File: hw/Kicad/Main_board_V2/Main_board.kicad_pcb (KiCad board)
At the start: 2 copper layers, 100 x 100 mm, 31 parts, among them J1 LIPO 2S, J10 DIST_FRONT, J11 SENSORES_LINEA, J12 DIST_DCHA, J2 MOT_IZQ, J3 TB6612FNG_A, J4 TB6612FNG_B, J5 DC-DC_5V, J6 HC-05, J7 MOT_DER, J8 DIST_IZQ, J9 CAMARA, SW1 SW_DPDT, SW2 SW_Push, SW3 SW_Push, U1 PCF8574

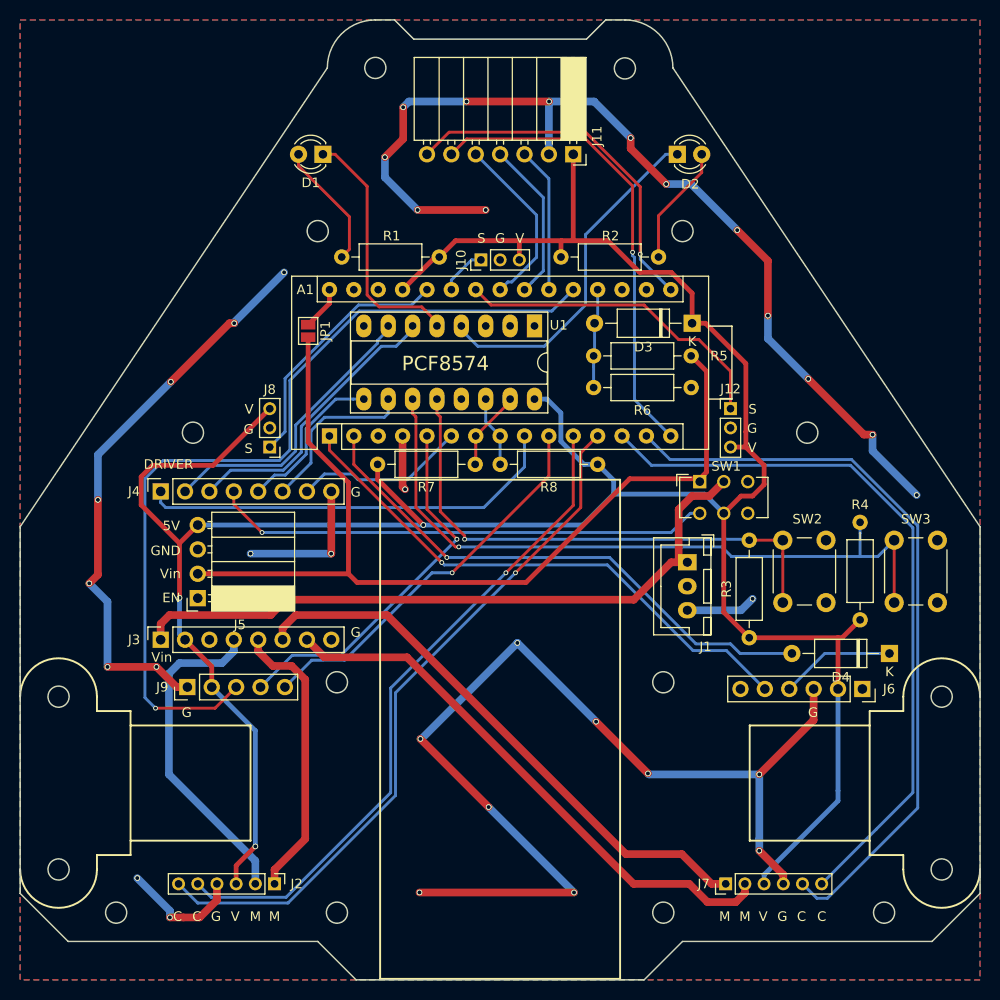
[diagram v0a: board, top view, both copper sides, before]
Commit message: Silkscreen fixed
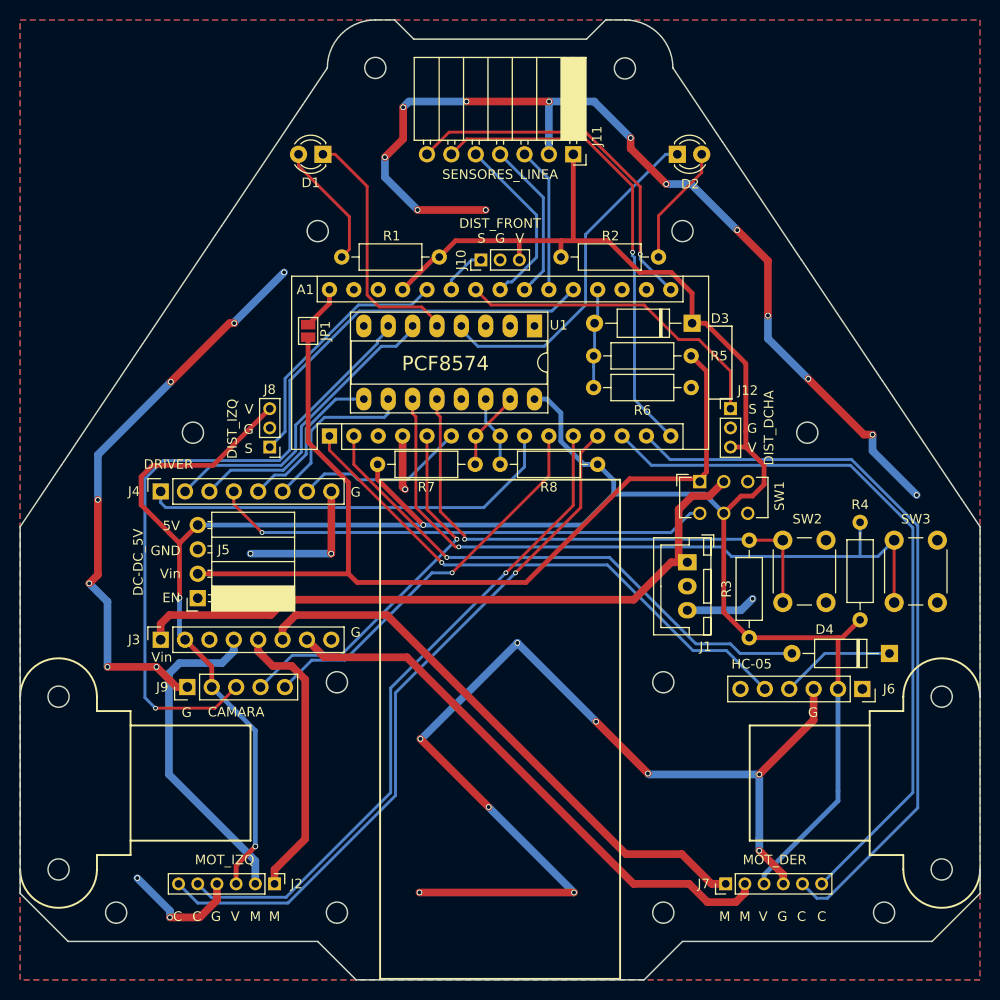
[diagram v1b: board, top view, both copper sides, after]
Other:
- board text added: "CAMARA"
- board text added: "DC-DC_5V"
- board text added: "DIST_DCHA"
- board text added: "DIST_FRONT"
- board text added: "DIST_IZQ"
- board text added: "HC-05"
- board text added: "MOT_DER"
- board text added: "MOT_IZQ"
- board text added: "SENSORES_LINEA"
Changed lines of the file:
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@@
-(kicad_pcb (version 4) (host pcbnew 4.0.7)
+(kicad_pcb (version 4) (host pcbnew 4.0.7+dfsg1-1ubuntu2)
   (general
     (links 94)
     (no_connects 0)
-    (area 99.924999 49.924999 200.075001 150.075001)
+    (area 99.899999 44.8 200.100001 150.100001)
     (thickness 1.6)
-    (drawings 127)
+    (drawings 136)
     (tracks 449)
     (zones 0)
@@
     (47 F.CrtYd user hide)
     (48 B.Fab user hide)
-    (49 F.Fab user hide)
+    (49 F.Fab user)
   )
   (setup
@@
       (effects (font (size 1 1) (thickness 0.15)))
     )
-    (fp_text value MOT_IZQ (at 0 12.06 270) (layer F.Fab)
+    (fp_text value MOT_IZQ (at -2.5 5.2 360) (layer F.Fab)
       (effects (font (size 1 1) (thickness 0.15)))
     )
@@
     (descr "Through hole angled socket strip, 1x04, 2.54mm pitch, 8.51mm socket length, single row (from Kicad 4.0.7), script generated")
     (tags "Through hole angled socket strip THT 1x04 2.54mm single row")
-    (fp_text reference J5 (at -4.38 -2.77 180) (layer F.SilkS)
+    (fp_text reference J5 (at -2.7 5.04 180) (layer F.SilkS)
       (effects (font (size 1 1) (thickness 0.15)))
     )
@@
       (effects (font (size 1 1) (thickness 0.15)))
     )
-    (fp_text value HC-05 (at 0 15.47 270) (layer F.Fab)
+    (fp_text value HC-05 (at -2.6 11.54 360) (layer F.Fab)
       (effects (font (size 1 1) (thickness 0.15)))
     )
@@
       (effects (font (size 1 1) (thickness 0.15)))
     )
-    (fp_text value MOT_DER (at 0 12.06 90) (layer F.Fab)
+    (fp_text value MOT_DER (at 2.5 5.1 180) (layer F.Fab)
       (effects (font (size 1 1) (thickness 0.15)))
     )
@@
       (effects (font (size 1 1) (thickness 0.15)))
     )
-    (fp_text value DIST_IZQ (at 0 6.06 180) (layer F.Fab)
+    (fp_text value DIST_IZQ (at 3.9 1.9 270) (layer F.Fab)
       (effects (font (size 1 1) (thickness 0.15)))
     )
@@
       (effects (font (size 1 1) (thickness 0.15)))
     )
-    (fp_text value CAMARA (at 0 12.49 90) (layer F.Fab)
+    (fp_text value CAMARA (at -2.6 5.08 180) (layer F.Fab)
       (effects (font (size 1 1) (thickness 0.15)))
     )
@@
       (effects (font (size 1 1) (thickness 0.15)))
     )
-    (fp_text value DIST_FRONT (at 0 6.06 90) (layer F.Fab)
+    (fp_text value DIST_FRONT (at 3.8 2 180) (layer F.Fab)
       (effects (font (size 1 1) (thickness 0.15)))
     )
@@
       (effects (font (size 1 1) (thickness 0.15)))
     )
-    (fp_text value SENSORES_LINEA (at -4.38 18.01 270) (layer F.Fab)
+    (fp_text value SENSORES_LINEA (at 2.1 7.62 360) (layer F.Fab)
       (effects (font (size 1 1) (thickness 0.15)))
     )
@@
     (descr "Through hole straight pin header, 1x03, 2.00mm pitch, single row")
     (tags "Through hole pin header THT 1x03 2.00mm single row")
-    (fp_text reference J12 (at 0 -2.06) (layer F.SilkS)
-      (effects (font (size 1 1) (thickness 0.15)))
-    )
-    (fp_text value DIST_DCHA (at 0 6.06) (layer F.Fab)
+    (fp_text reference J12 (at 1.8 -1.9) (layer F.SilkS)
+      (effects (font (size 1 1) (thickness 0.15)))
+    )
+    (fp_text value DIST_DCHA (at 4 2 90) (layer F.Fab)
       (effects (font (size 1 1) (thickness 0.15)))
     )
@@
     (descr "CuK sub miniature slide switch, JS series, DPDT, right angle, http://www.ckswitches.com/media/1422/js.pdf")
     (tags "switch DPDT")
-    (fp_text reference SW1 (at 2.75 -1.6) (layer F.SilkS)
+    (fp_text reference SW1 (at 8.3 1.5 90) (layer F.SilkS)
       (effects (font (size 1 1) (thickness 0.15)))
     )
@@
     (descr "D, A-405 series, Axial, Horizontal, pin pitch=10.16mm, , length*diameter=5.2*2.7mm^2, , http://www.diodes.com/_files/packages/A-405.pdf")
     (tags "D A-405 series Axial Horizontal pin pitch 10.16mm  length 5.2mm diameter 2.7mm")
-    (fp_text reference D3 (at 5.08 -2.47 180) (layer F.SilkS)
+    (fp_text reference D3 (at -2.9 0.5 180) (layer F.SilkS)
       (effects (font (size 1 1) (thickness 0.15)))
     )
@@
       (effects (font (size 1 1) (thickness 0.15)))
     )
-    (fp_text user K (at 0 -1.9 180) (layer F.SilkS)
+    (fp_text user K (at 0 -1.9 180) (layer F.SilkS) hide
       (effects (font (size 1 1) (thickness 0.15)))
     )
@@
     (descr "D, A-405 series, Axial, Horizontal, pin pitch=10.16mm, , length*diameter=5.2*2.7mm^2, , http://www.diodes.com/_files/packages/A-405.pdf")
     (tags "D A-405 series Axial Horizontal pin pitch 10.16mm  length 5.2mm diameter 2.7mm")
-    (fp_text reference D4 (at 5.08 -2.47 180) (layer F.SilkS)
+    (fp_text reference D4 (at 6.76 2.5 180) (layer F.SilkS)
       (effects (font (size 1 1) (thickness 0.15)))
     )
@@
       (effects (font (size 1 1) (thickness 0.15)))
     )
-    (fp_text user K (at 0 -1.9 180) (layer F.SilkS)
+    (fp_text user K (at 0 -1.9 180) (layer F.SilkS) hide
       (effects (font (size 1 1) (thickness 0.15)))
     )
@@
     )
   )
+  (gr_text CAMARA (at 122.5 122.1) (layer F.SilkS)
+    (effects (font (size 1 1) (thickness 0.15)))
+  )
+  (gr_text DC-DC_5V (at 112.3 106.5 90) (layer F.SilkS)
+    (effects (font (size 1 1) (thickness 0.15)))
+  )
+  (gr_text DIST_IZQ (at 122.1 92.6 90) (layer F.SilkS)
+    (effects (font (size 1 1) (thickness 0.15)))
+  )
+  (gr_text SENSORES_LINEA (at 150 66.1) (layer F.SilkS)
+    (effects (font (size 1 1) (thickness 0.15)))
+  )
+  (gr_text DIST_FRONT (at 150 71.2) (layer F.SilkS)
+    (effects (font (size 1 1) (thickness 0.15)))
+  )
+  (gr_text DIST_DCHA (at 178 92.5 90) (layer F.SilkS)
+    (effects (font (size 1 1) (thickness 0.15)))
+  )
+  (gr_text HC-05 (at 176.2 117.1) (layer F.SilkS)
+    (effects (font (size 1 1) (thickness 0.15)))
+  )
+  (gr_text MOT_DER (at 178.6 137.5) (layer F.SilkS)
+    (effects (font (size 1 1) (thickness 0.15)))
+  )
+  (gr_text MOT_IZQ (at 121.3 137.5) (layer F.SilkS)
+    (effects (font (size 1 1) (thickness 0.15)))
+  )
   (gr_text "Puma Pride\nRobotics Team" (at 150 143) (layer B.SilkS)
